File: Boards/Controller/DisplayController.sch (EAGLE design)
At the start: 46 parts, among them J1 USB0001LF, J3 AVR_SPI_PRG_62X3_LOCK, Q1 BSS138, U1 MCP1703CB, U100 MCP73831, U101 MAX1797, U2 FT232RQ, U3 ATMEGA328P-MU, U5 MAX1704X, X2 CRYSTAL7A-20.000MAAJ-T

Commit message: updated layout for controller.
Signed-off-by: Evan Richardson <erichardson@savi.com>
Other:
- note added: "3.7->5V Boost"
- note added: "Fuel Guage"
- note added: "LED Display Controller"
- note added: "Microcontroller"
- note added: "USB"
- note removed: "3.7->5V STEP UP"
- note removed: "MICROCONTROLLER"

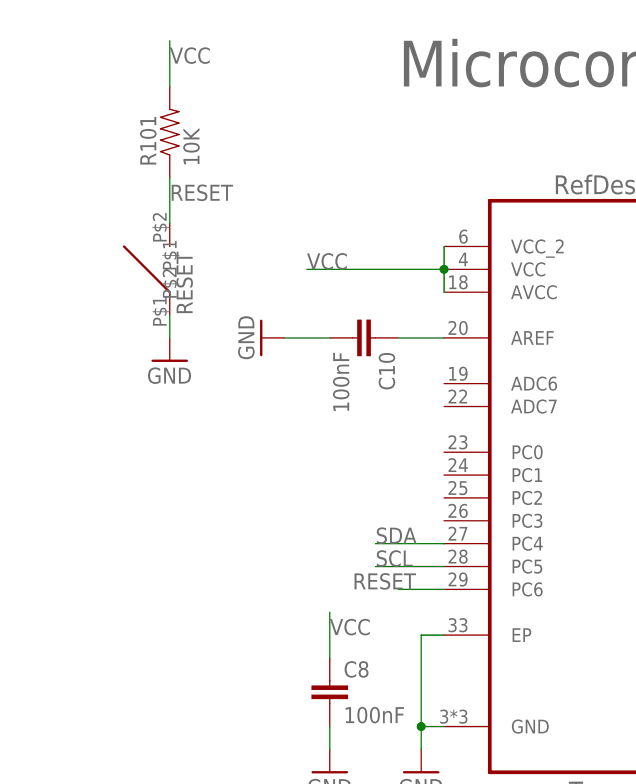
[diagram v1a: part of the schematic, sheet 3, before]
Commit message: Added Thermistor to determine board temperature Cleaned up thermal vias and traces under ICs
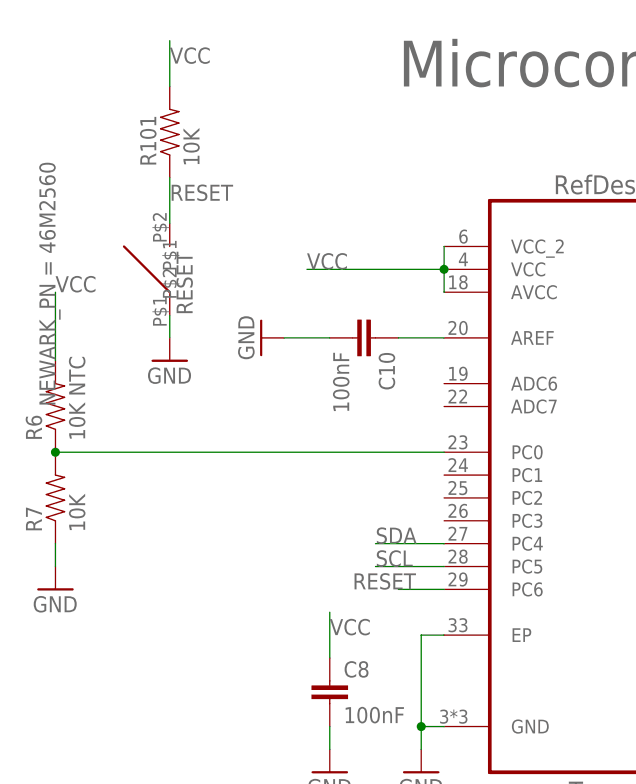
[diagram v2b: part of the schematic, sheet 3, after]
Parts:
- added R6: 10K NTC, SparkFun:RESISTOR0603-RES
- added R7: 10K, SparkFun:RESISTOR0603-RES
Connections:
- new net N$18: R6.1, R7.2, U3.PC0
- net GND: now also R7.1
- net VCC: now also R6.2
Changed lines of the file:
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@@
 <grid distance="0.1" unitdist="inch" unit="inch" style="lines" multiple="1" display="no" altdistance="0.01" altunitdist="inch" altunit="inch"/>
 <layers>
-<layer number="1" name="Top" color="4" fill="1" visible="no" active="no"/>
-<layer number="2" name="Route2" color="1" fill="3" visible="no" active="no"/>
-<layer number="3" name="Route3" color="4" fill="3" visible="no" active="no"/>
-<layer number="4" name="Route4" color="1" fill="4" visible="no" active="no"/>
-<layer number="5" name="Route5" color="4" fill="4" visible="no" active="no"/>
-<layer number="6" name="Route6" color="1" fill="8" visible="no" active="no"/>
-<layer number="7" name="Route7" color="4" fill="8" visible="no" active="no"/>
-<layer number="8" name="Route8" color="1" fill="2" visible="no" active="no"/>
-<layer number="9" name="Route9" color="4" fill="2" visible="no" active="no"/>
-<layer number="10" name="Route10" color="1" fill="7" visible="no" active="no"/>
-<layer number="11" name="Route11" color="4" fill="7" visible="no" active="no"/>
-<layer number="12" name="Route12" color="1" fill="5" visible="no" active="no"/>
-<layer number="13" name="Route13" color="4" fill="5" visible="no" active="no"/>
-<layer number="14" name="Route14" color="1" fill="6" visible="no" active="no"/>
-<layer number="15" name="Route15" color="4" fill="6" visible="no" active="no"/>
-<layer number="16" name="Bottom" color="1" fill="1" visible="no" active="no"/>
-<layer number="17" name="Pads" color="2" fill="1" visible="no" active="no"/>
-<layer number="18" name="Vias" color="2" fill="1" visible="no" active="no"/>
-<layer number="19" name="Unrouted" color="6" fill="1" visible="no" active="no"/>
-<layer number="20" name="Dimension" color="15" fill="1" visible="no" active="no"/>
-<layer number="21" name="tPlace" color="7" fill="1" visible="no" active="no"/>
-<layer number="22" name="bPlace" color="7" fill="1" visible="no" active="no"/>
-<layer number="23" name="tOrigins" color="15" fill="1" visible="no" active="no"/>
-<layer number="24" name="bOrigins" color="15" fill="1" visible="no" active="no"/>
-<layer number="25" name="tNames" color="7" fill="1" visible="no" active="no"/>
-<layer number="26" name="bNames" color="7" fill="1" visible="no" active="no"/>
-<layer number="27" name="tValues" color="7" fill="1" visible="no" active="no"/>
-<layer number="28" name="bValues" color="7" fill="1" visible="no" active="no"/>
+<layer number="1" name="Top" color="4" fill="1" visible="yes" active="no"/>
+<layer number="2" name="Route2" color="1" fill="3" visible="yes" active="no"/>
+<layer number="3" name="Route3" color="4" fill="3" visible="yes" active="no"/>
+<layer number="4" name="Route4" color="1" fill="4" visible="yes" active="no"/>
+<layer number="5" name="Route5" color="4" fill="4" visible="yes" active="no"/>
+<layer number="6" name="Route6" color="1" fill="8" visible="yes" active="no"/>
+<layer number="7" name="Route7" color="4" fill="8" visible="yes" active="no"/>
+<layer number="8" name="Route8" color="1" fill="2" visible="yes" active="no"/>
+<layer number="9" name="Route9" color="4" fill="2" visible="yes" active="no"/>
+<layer number="10" name="Route10" color="1" fill="7" visible="yes" active="no"/>
+<layer number="11" name="Route11" color="4" fill="7" visible="yes" active="no"/>
+<layer number="12" name="Route12" color="1" fill="5" visible="yes" active="no"/>
+<layer number="13" name="Route13" color="4" fill="5" visible="yes" active="no"/>
+<layer number="14" name="Route14" color="1" fill="6" visible="yes" active="no"/>
+<layer number="15" name="Route15" color="4" fill="6" visible="yes" active="no"/>
+<layer number="16" name="Bottom" color="1" fill="1" visible="yes" active="no"/>
+<layer number="17" name="Pads" color="2" fill="1" visible="yes" active="no"/>
+<layer number="18" name="Vias" color="2" fill="1" visible="yes" active="no"/>
+<layer number="19" name="Unrouted" color="6" fill="1" visible="yes" active="no"/>
+<layer number="20" name="Dimension" color="15" fill="1" visible="yes" active="no"/>
+<layer number="21" name="tPlace" color="7" fill="1" visible="yes" active="no"/>
+<layer number="22" name="bPlace" color="7" fill="1" visible="yes" active="no"/>
+<layer number="23" name="tOrigins" color="15" fill="1" visible="yes" active="no"/>
+<layer number="24" name="bOrigins" color="15" fill="1" visible="yes" active="no"/>
+<layer number="25" name="tNames" color="7" fill="1" visible="yes" active="no"/>
+<layer number="26" name="bNames" color="7" fill="1" visible="yes" active="no"/>
+<layer number="27" name="tValues" color="7" fill="1" visible="yes" active="no"/>
+<layer number="28" name="bValues" color="7" fill="1" visible="yes" active="no"/>
 <layer number="29" name="tStop" color="7" fill="3" visible="no" active="no"/>
 <layer number="30" name="bStop" color="7" fill="6" visible="no" active="no"/>
@@
 <layer number="35" name="tGlue" color="7" fill="4" visible="no" active="no"/>
 <layer number="36" name="bGlue" color="7" fill="5" visible="no" active="no"/>
-<layer number="37" name="tTest" color="7" fill="1" visible="no" active="no"/>
-<layer number="38" name="bTest" color="7" fill="1" visible="no" active="no"/>
+<layer number="37" name="tTest" color="7" fill="1" visible="yes" active="no"/>
+<layer number="38" name="bTest" color="7" fill="1" visible="yes" active="no"/>
 <layer number="39" name="tKeepout" color="4" fill="11" visible="no" active="no"/>
 <layer number="40" name="bKeepout" color="1" fill="11" visible="no" active="no"/>
@@
 <layer number="44" name="Drills" color="7" fill="1" visible="no" active="no"/>
 <layer number="45" name="Holes" color="7" fill="1" visible="no" active="no"/>
-<layer number="46" name="Milling" color="3" fill="1" visible="no" active="no"/>
-<layer number="47" name="Measures" color="7" fill="1" visible="no" active="no"/>
-<layer number="48" name="Document" color="7" fill="1" visible="no" active="no"/>
-<layer number="49" name="Reference" color="7" fill="1" visible="no" active="no"/>
-<layer number="50" name="dxf" color="7" fill="1" visible="no" active="no"/>
-<layer number="51" name="tDocu" color="7" fill="1" visible="no" active="no"/>
-<layer number="52" name="bDocu" color="7" fill="1" visible="no" active="no"/>
-<layer number="53" name="tGND_GNDA" color="7" fill="9" visible="no" active="no"/>
-<layer number="54" name="bGND_GNDA" color="1" fill="9" visible="no" active="no"/>
-<layer number="56" name="wert" color="7" fill="1" visible="no" active="no"/>
+<layer number="46" name="Milling" color="3" fill="1" visible="yes" active="no"/>
+<layer number="47" name="Measures" color="7" fill="1" visible="yes" active="no"/>
+<layer number="48" name="Document" color="7" fill="1" visible="yes" active="no"/>
+<layer number="49" name="Reference" color="7" fill="1" visible="yes" active="no"/>
+<layer number="50" name="dxf" color="7" fill="1" visible="yes" active="no"/>
+<layer number="51" name="tDocu" color="7" fill="1" visible="yes" active="no"/>
+<layer number="52" name="bDocu" color="7" fill="1" visible="yes" active="no"/>
+<layer number="53" name="tGND_GNDA" color="7" fill="9" visible="yes" active="no"/>
+<layer number="54" name="bGND_GNDA" color="1" fill="9" visible="yes" active="no"/>
+<layer number="56" name="wert" color="7" fill="1" visible="yes" active="no"/>
 <layer number="91" name="Nets" color="2" fill="1" visible="yes" active="yes"/>
 <layer number="92" name="Busses" color="1" fill="1" visible="yes" active="yes"/>
@@
 <part name="FRAME2" library="SparkFun" deviceset="FRAME-LETTER" device=""/>
 <part name="FRAME3" library="SparkFun" deviceset="FRAME-LETTER" device=""/>
+<part name="R6" library="SparkFun" deviceset="RESISTOR" device="0603-RES" value="10K NTC">
+<attribute name="NEWARK_PN" value="46M2560"/>
+</part>
+<part name="R7" library="SparkFun" deviceset="RESISTOR" device="0603-RES" value="10K"/>
+<part name="GND15" library="SparkFun" deviceset="GND" device=""/>
 </parts>
 <sheets>
@@
 <instance part="S100" gate="1" x="185.42" y="53.34"/>
 <instance part="U1" gate="G$1" x="182.88" y="157.48">
-<attribute name="NEWARKPN" x="182.88" y="157.48" size="1.778" layer="96"/>
+<attribute name="NEWARKPN" x="178.816" y="163.576" size="1.778" layer="96"/>
 </instance>
 <instance part="C3" gate="G$1" x="200.66" y="152.4">
@@
 <instance part="C12" gate="G$1" x="149.86" y="91.44"/>
 <instance part="GND13" gate="1" x="149.86" y="83.82"/>
+<instance part="R6" gate="G$1" x="10.16" y="106.68" rot="R90">
+<attribute name="NEWARK_PN" x="10.16" y="106.68" size="1.778" layer="96" rot="R90" display="both"/>
+</instance>
+<instance part="R7" gate="G$1" x="10.16" y="96.52" rot="R90"/>
+<instance part="GND15" gate="1" x="10.16" y="86.36"/>
 </instances>
 <busses>
@@
 <wire x1="149.86" y1="88.9" x2="149.86" y2="86.36" width="0.1524" layer="91"/>
 </segment>
+<segment>
+<pinref part="R7" gate="G$1" pin="1"/>
+<pinref part="GND15" gate="1" pin="GND"/>
+<wire x1="10.16" y1="88.9" x2="10.16" y2="91.44" width="0.1524" layer="91"/>
+</segment>
 </net>
 <net name="VCC" class="0">
@@
 <pinref part="R5" gate="G$1" pin="1"/>
 </segment>
+<segment>
+<pinref part="R6" gate="G$1" pin="2"/>
+<wire x1="10.16" y1="111.76" x2="10.16" y2="119.38" width="0.1524" layer="91"/>
+<label x="10.16" y="119.38" size="1.778" layer="95"/>
+</segment>
 </net>
 <net name="D2" class="0">
@@
 </segment>
 </net>
+<net name="N$18" class="0">
+<segment>
+<pinref part="U3" gate="A" pin="PC0"/>
+<wire x1="53.34" y1="101.6" x2="10.16" y2="101.6" width="0.1524" layer="91"/>
+<pinref part="R7" gate="G$1" pin="2"/>
+<pinref part="R6" gate="G$1" pin="1"/>
+<junction x="10.16" y="101.6"/>
+</segment>
+</net>
 </nets>
 </sheet>
 </sheets>
-<errors>
-</errors>
 </schematic>
 </drawing>

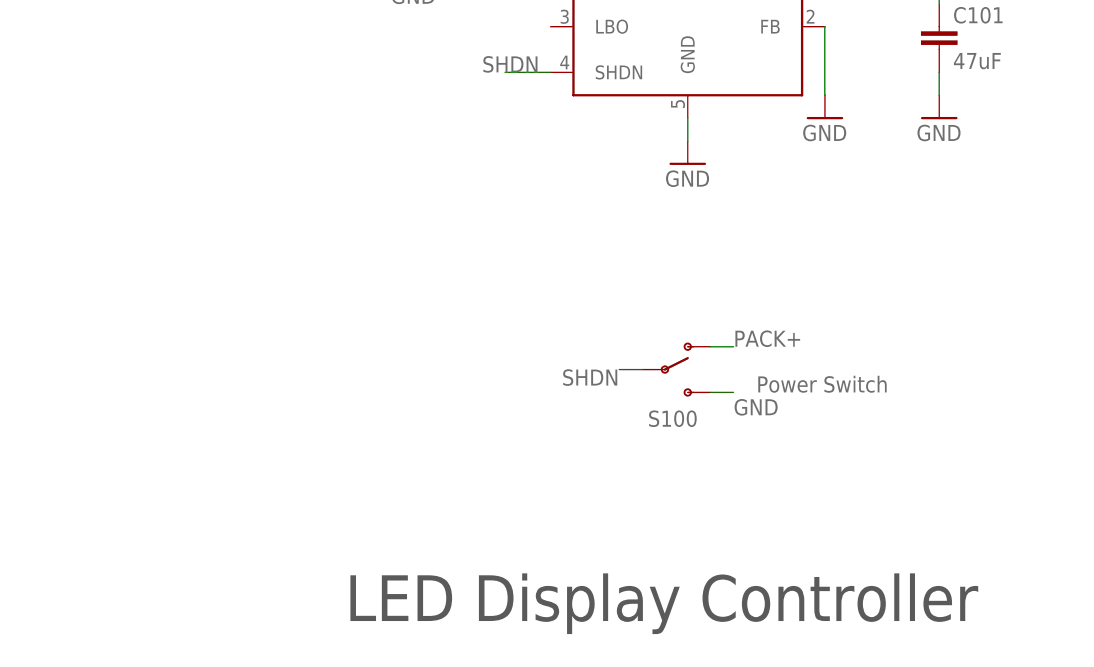
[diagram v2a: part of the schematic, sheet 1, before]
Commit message: cleaned up controller traces replaced power switch with new part from sparkfun (deprecated old switch) removed thermistor (nice to have but not really needed for now)
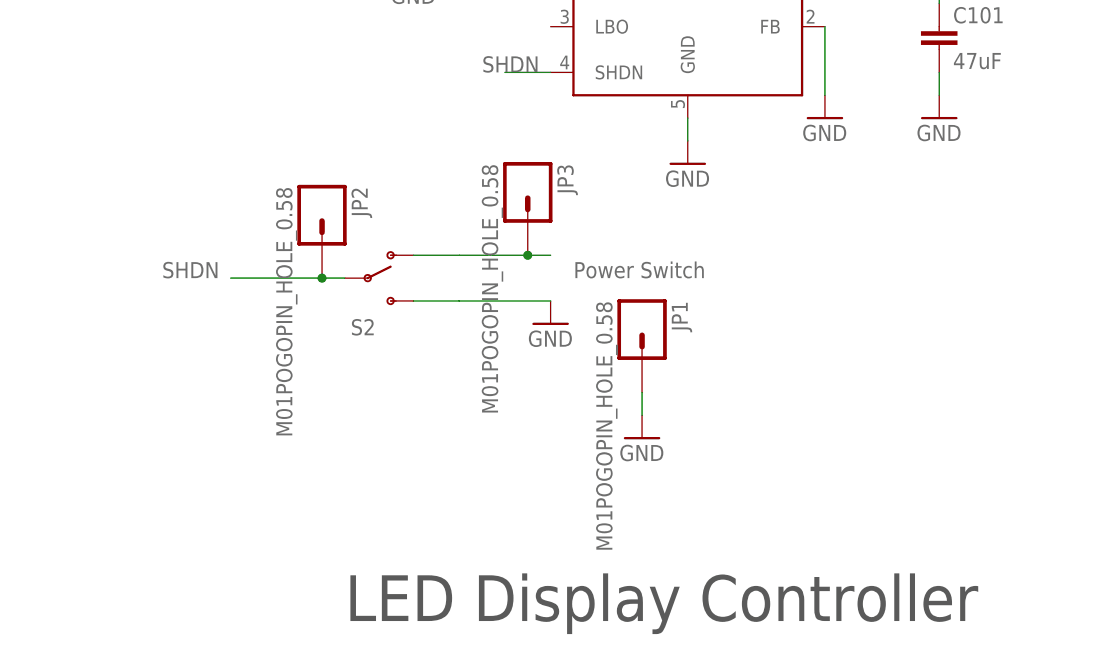
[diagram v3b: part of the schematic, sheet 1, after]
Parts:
- removed R6: 10K NTC, SparkFun:RESISTOR0603-RES
- removed R7: 10K, SparkFun:RESISTOR0603-RES
- removed S100: (no value), SparkFun:SWITCH-SPSTSMD2
- added JP1, JP2, JP3: M01POGOPIN_HOLE_0.58, SparkFun-Connectors:M01POGOPIN_HOLE_0.58
- added S2: (no value), SparkFun-Electromechanical:SWITCH-SPDT-SMD-A
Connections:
- removed net N$18: R6.1, R7.2, U3.PC0
- net GND: now also JP1.1, S2.S; no longer R7.1, S100.S
- net PACK+: now also JP3.1, S2.O; no longer S100.O
- net SHDN: now also JP2.1, S2.P; no longer S100.P
- net VCC: no longer R6.2

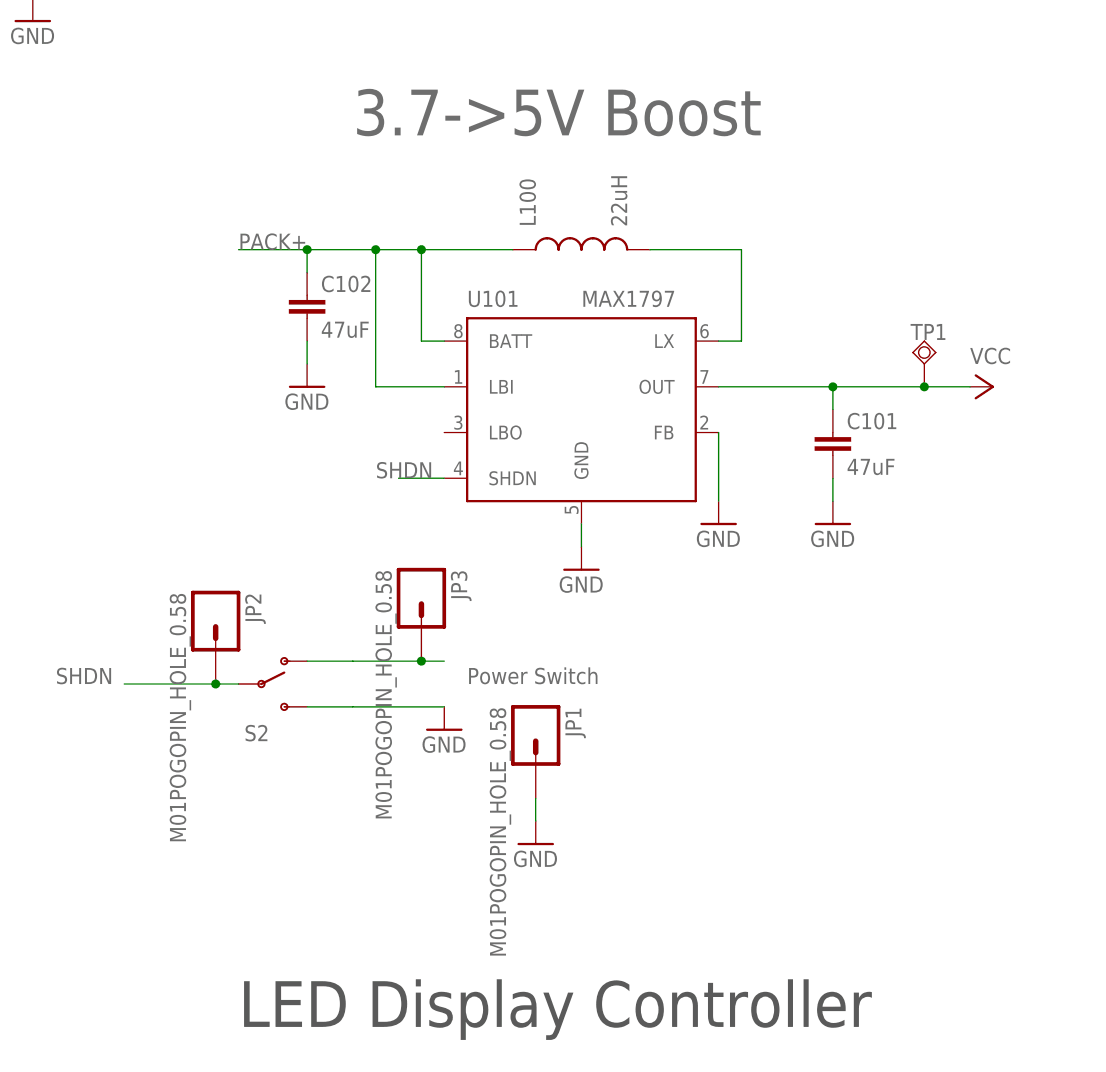
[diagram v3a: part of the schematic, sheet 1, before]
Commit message: moved Power supplies to top side cleaned up traces moved reset switch near display connector Added various Newark part numbers to board parts
Signed-off-by: evanrich <erichardson@savi.com>
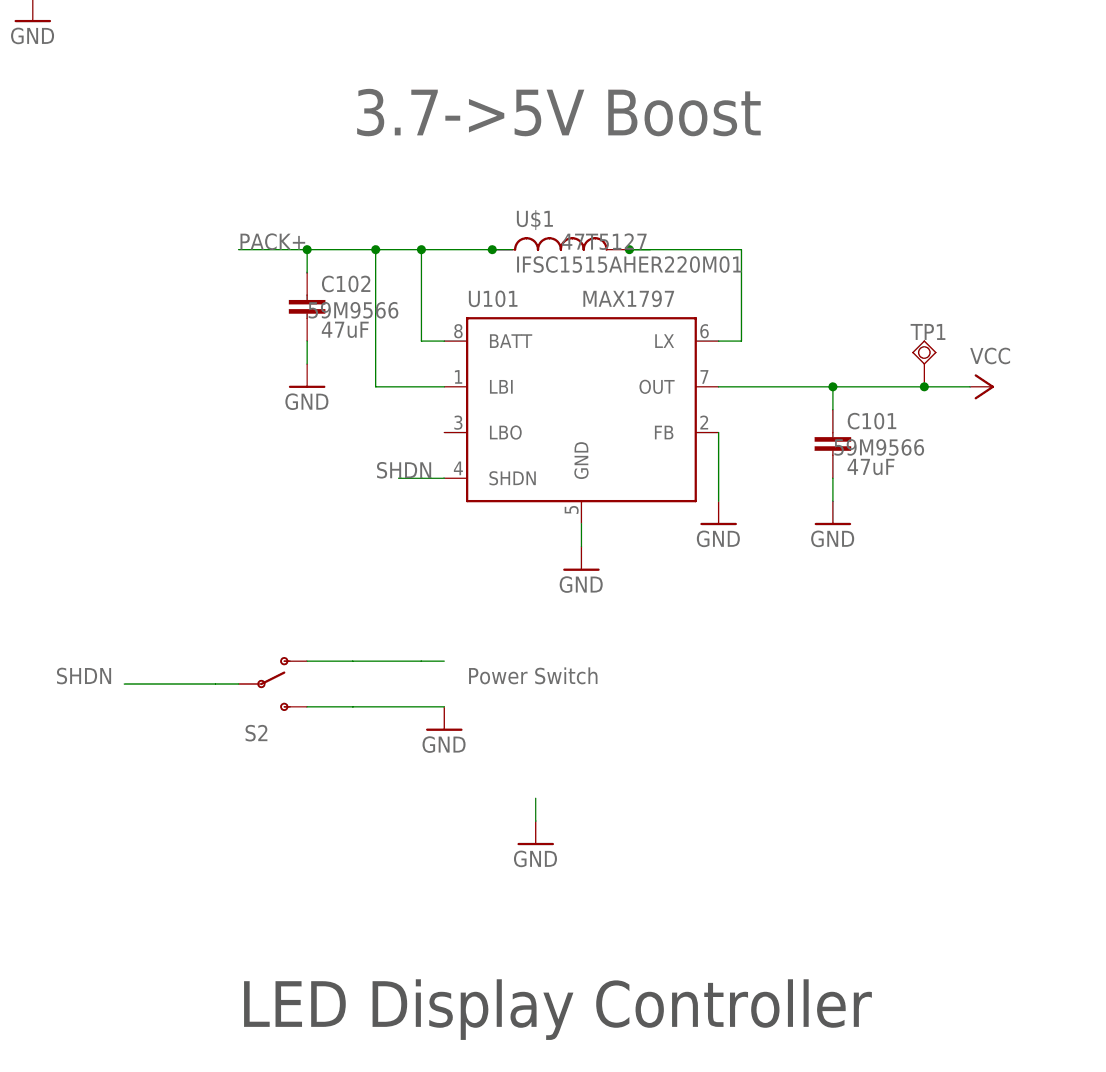
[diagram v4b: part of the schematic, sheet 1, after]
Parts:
- removed JP1, JP2, JP3: M01POGOPIN_HOLE_0.58, SparkFun-Connectors:M01POGOPIN_HOLE_0.58
- removed L100: 22uH, MyParts:INDUCTORSD53
- added U$1: IFSC1515AHER220M01, MyParts:IFSC1515AHER220M01
- C101, C102: device SparkFun:CAP0805 -> SparkFun:CAP1206; NEWARK_PN (none) -> 59M9566
- RN2: OC_NEWARK unknown -> 15M6872
- RN3: OC_NEWARK (none) -> 15M6870
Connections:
- net GND: no longer JP1.1
- net N$10: now also RN1B.2; no longer RN1A.2
- net N$24: now also U$1.2; no longer L100.2
- net N$3: now also RN1B.1; no longer RN1A.1
- net N$4: now also RN1C.1; no longer RN1B.1
- net N$6: now also RN1C.2; no longer RN1B.2
- net PACK+: now also U$1.1; no longer JP3.1, L100.1
- net SHDN: no longer JP2.1
